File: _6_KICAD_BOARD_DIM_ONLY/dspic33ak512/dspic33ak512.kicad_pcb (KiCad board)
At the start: 2 copper layers, 114 x 82 mm, 28 parts, among them J1 HTEC8-160-01-X-DV-A-BL-X, J2 PH2-20-UA, J3 PH2-20-UA, J4 PH2-20-UA, J5 PH2-20-UA, J6 PH2-20-UA, U1 AZ1117H-3.3TRE1, U3 DAC7564ICPW, U4 FM24W256G

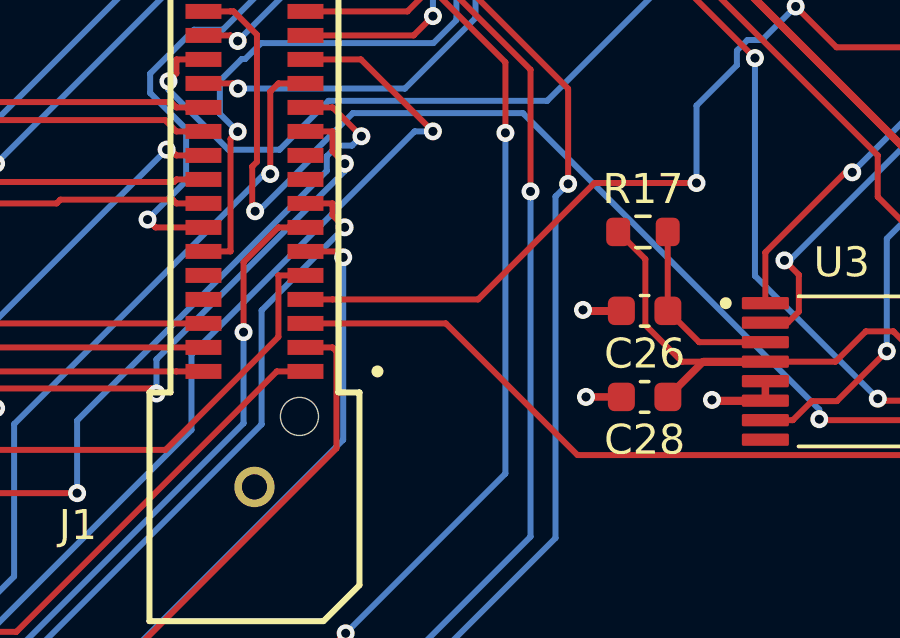
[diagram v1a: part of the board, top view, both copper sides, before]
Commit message: feat : i2c 핀이 뒤집혀있어 fram 동작 불가 pic48 new board 또는, aux핀을 통해서 진행예정
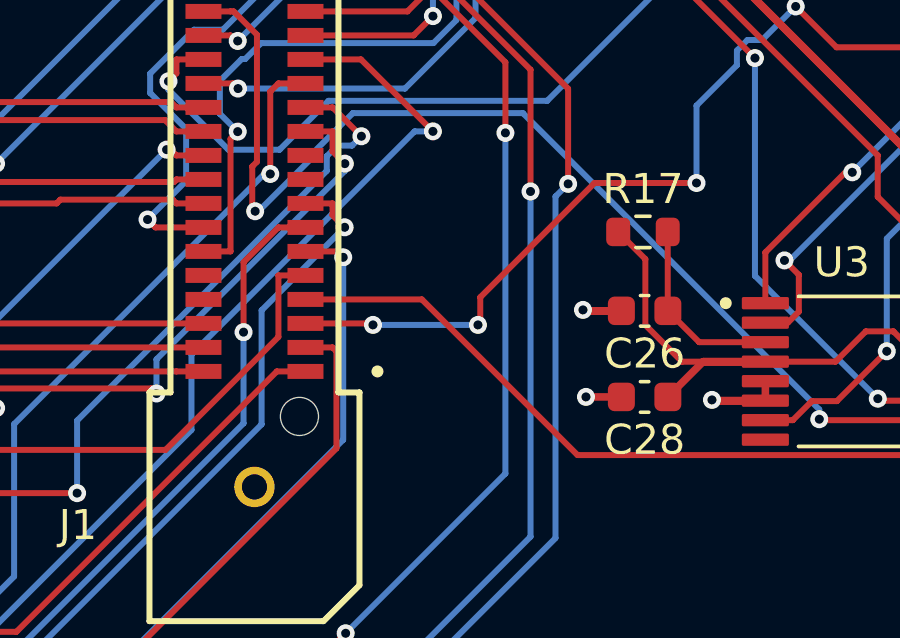
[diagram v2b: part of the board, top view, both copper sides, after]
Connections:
- J1 pad 5: /DIM_SHEET/I2C_BUS.SDA -> /DIM_SHEET/I2C_BUS.SCL
- J1 pad 7: /DIM_SHEET/I2C_BUS.SCL -> /DIM_SHEET/I2C_BUS.SDA
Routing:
- net /DIM_SHEET/I2C_BUS.SCL: track 40.2 -> 41.0 mm, vias 2 -> 4
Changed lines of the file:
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@@
 			(size 0.5 1.2)
 			(layers "F.Cu" "F.Mask" "F.Paste")
-			(net 95 "/DIM_SHEET/I2C_BUS.SDA")
+			(net 99 "/DIM_SHEET/I2C_BUS.SCL")
 			(pinfunction "5")
 			(pintype "passive")
@@
 			(size 0.5 1.2)
 			(layers "F.Cu" "F.Mask" "F.Paste")
-			(net 99 "/DIM_SHEET/I2C_BUS.SCL")
+			(net 95 "/DIM_SHEET/I2C_BUS.SDA")
 			(pinfunction "7")
 			(pintype "passive")
@@
 	)
 	(segment
-		(start 121.2708 106.8385)
-		(end 129.18 98.9293)
+		(start 129.18 93.3)
+		(end 131.7 93.3)
 		(width 0.2)
 		(layer "F.Cu")
@@
 	)
 	(segment
-		(start 129.18 93.3)
-		(end 131.7 93.3)
+		(start 129.18 98.9293)
+		(end 129.18 93.3)
 		(width 0.2)
 		(layer "F.Cu")
@@
 	)
 	(segment
-		(start 103.9299 102.45)
+		(start 103.1299 101.65)
 		(end 108.3184 106.8385)
 		(width 0.2)
@@
 	)
 	(segment
-		(start 129.18 98.9293)
-		(end 129.18 93.3)
+		(start 128.85 92.64)
+		(end 129.18 92.97)
 		(width 0.2)
 		(layer "F.Cu")
@@
 	)
 	(segment
-		(start 128.85 92.64)
-		(end 129.18 92.97)
+		(start 121.2708 106.8385)
+		(end 129.18 98.9293)
 		(width 0.2)
 		(layer "F.Cu")
@@
 	)
 	(segment
-		(start 99.25 102.45)
-		(end 103.9299 102.45)
+		(start 99.25 101.65)
+		(end 103.1299 101.65)
 		(width 0.2)
 		(layer "F.Cu")
@@
 	)
 	(segment
+		(start 105.0772 102.4228)
+		(end 105 102.5)
+		(width 0.2)
+		(layer "F.Cu")
+		(net 99)
+	)
+	(segment
+		(start 101.45 102.45)
+		(end 101.5 102.5)
+		(width 0.2)
+		(layer "F.Cu")
+		(net 99)
+	)
+	(segment
 		(start 130.43 91.37)
 		(end 131.7 90.1)
@@
 	)
 	(segment
-		(start 105.0044 101.65)
+		(start 105.0772 101.5772)
 		(end 108.8854 97.769)
 		(width 0.2)
@@
 	)
 	(segment
-		(start 128.85 91.37)
-		(end 130.43 91.37)
+		(start 99.25 102.45)
+		(end 101.45 102.45)
 		(width 0.2)
 		(layer "F.Cu")
@@
 	)
 	(segment
-		(start 108.8854 97.769)
-		(end 108.8854 97.7689)
+		(start 128.85 91.37)
+		(end 130.43 91.37)
 		(width 0.2)
 		(layer "F.Cu")
@@
 	)
 	(segment
-		(start 99.25 101.65)
-		(end 100.1517 101.65)
+		(start 108.8854 97.769)
+		(end 108.8854 97.7689)
 		(width 0.2)
 		(layer "F.Cu")
@@
 	)
 	(segment
-		(start 100.1517 101.65)
-		(end 105.0044 101.65)
+		(start 105.0772 101.5772)
+		(end 105.0772 102.4228)
 		(width 0.2)
 		(layer "F.Cu")
@@
 	)
 	(via
+		(at 105 102.5)
+		(size 0.6)
+		(drill 0.3)
+		(layers "F.Cu" "B.Cu")
+		(net 99)
+	)
+	(via
 		(at 112.2849 97.7689)
 		(size 0.6)
@@
 	)
 	(via
+		(at 101.5 102.5)
+		(size 0.6)
+		(drill 0.3)
+		(layers "F.Cu" "B.Cu")
+		(net 99)
+	)
+	(via
 		(at 115.5903 91.8842)
 		(size 0.6)
@@
 		(width 0.2)
 		(layer "B.Cu")
+		(net 99)
+	)
+	(segment
+		(start 105 102.5)
+		(end 101.5 102.5)
+		(width 0.2)
+		(layer "B.Cu")
